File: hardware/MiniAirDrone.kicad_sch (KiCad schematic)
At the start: 29 parts, among them J1 USB_C_Receptacle_USB2.0, Q1 UMH3N, U1 CH340C, U2 ESP32-WROOM-32, U3 MPU-6050, U4 MS5611-01BA, U5 VL53L1CXV0FY1, U6 TS1117BCW33_RPG

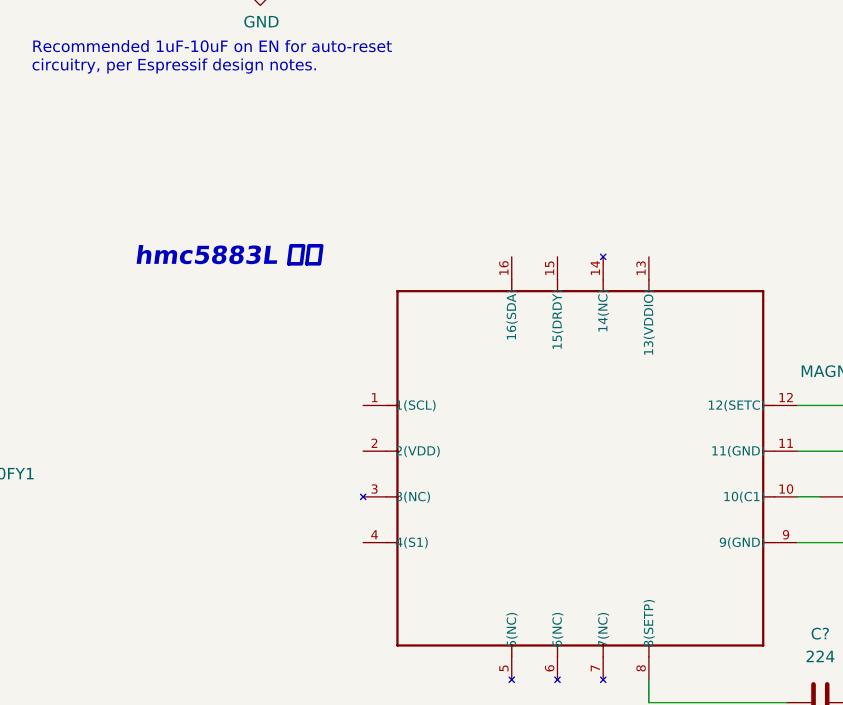
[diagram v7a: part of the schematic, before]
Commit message: Update MiniAirDrone.kicad_sch
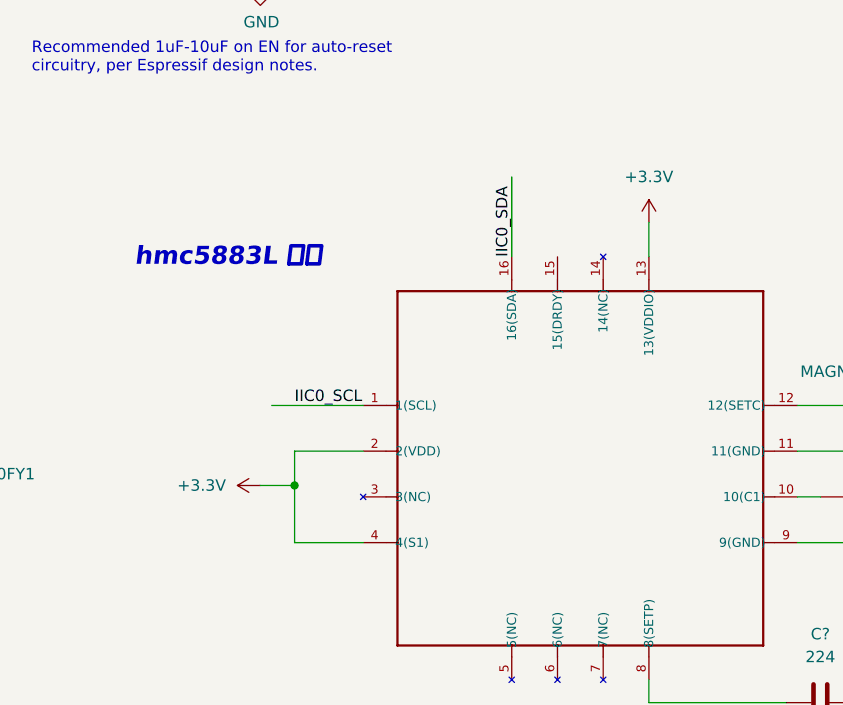
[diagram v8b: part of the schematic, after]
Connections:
- net +3.3V: now also U?.13 (13(VDDIO)), U?.2 (2(VDD)), U?.4 (4(S1))
- net IIC0_SCL: now also U?.1 (1(SCL))
- net IIC0_SDA: now also U?.16 (16(SDA))
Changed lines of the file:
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@@
   (junction (at 185.42 53.34) (diameter 0) (color 0 0 0 0)
+  )
+  (junction (at 241.3 109.22) (diameter 0) (color 0 0 0 0)
   )
   (junction (at 50.8 91.44) (diameter 0) (color 0 0 0 0)
@@
     (stroke (width 0) (type default) (color 0 0 0 0))
   )
+  (wire (pts (xy 241.3 115.57) (xy 241.3 109.22))
+    (stroke (width 0) (type default) (color 0 0 0 0))
+  )
+  (wire (pts (xy 238.76 100.33) (xy 248.92 100.33))
+    (stroke (width 0) (type default) (color 0 0 0 0))
+  )
   (wire (pts (xy 373.38 77.47) (xy 392.43 77.47))
     (stroke (width 0) (type default) (color 0 0 0 0))
@@
     (stroke (width 0) (type default) (color 0 0 0 0))
   )
+  (wire (pts (xy 265.43 74.93) (xy 265.43 83.82))
+    (stroke (width 0) (type default) (color 0 0 0 0))
+  )
   (wire (pts (xy 367.03 146.05) (xy 367.03 148.59))
     (stroke (width 0) (type default) (color 0 0 0 0))
@@
     (stroke (width 0) (type default) (color 0 0 0 0))
   )
+  (wire (pts (xy 280.67 80.01) (xy 280.67 83.82))
+    (stroke (width 0) (type default) (color 0 0 0 0))
+  )
   (wire (pts (xy 358.14 107.95) (xy 358.14 110.49))
     (stroke (width 0) (type default) (color 0 0 0 0))
@@
     (stroke (width 0) (type default) (color 0 0 0 0))
   )
+  (wire (pts (xy 248.92 115.57) (xy 241.3 115.57))
+    (stroke (width 0) (type default) (color 0 0 0 0))
+  )
   (wire (pts (xy 34.29 67.31) (xy 26.67 67.31))
     (stroke (width 0) (type default) (color 0 0 0 0))
@@
     (stroke (width 0) (type default) (color 0 0 0 0))
   )
+  (wire (pts (xy 241.3 105.41) (xy 248.92 105.41))
+    (stroke (width 0) (type default) (color 0 0 0 0))
+  )
   (wire (pts (xy 297.18 115.57) (xy 308.61 115.57))
     (stroke (width 0) (type default) (color 0 0 0 0))
@@
     (stroke (width 0) (type default) (color 0 0 0 0))
   )
+  (wire (pts (xy 241.3 109.22) (xy 241.3 105.41))
+    (stroke (width 0) (type default) (color 0 0 0 0))
+  )
   (wire (pts (xy 129.54 115.57) (xy 116.84 115.57))
     (stroke (width 0) (type default) (color 0 0 0 0))
@@
   )
   (wire (pts (xy 339.09 30.48) (xy 330.2 30.48))
+    (stroke (width 0) (type default) (color 0 0 0 0))
+  )
+  (wire (pts (xy 237.49 109.22) (xy 241.3 109.22))
     (stroke (width 0) (type default) (color 0 0 0 0))
   )
@@
     (effects (font (size 1.27 1.27)) (justify right bottom))
   )
+  (label "IIC0_SCL" (at 241.3 100.33 0)
+    (effects (font (size 1.27 1.27)) (justify left bottom))
+  )
   (label "IIC0_SDA" (at 96.52 101.6 0)
     (effects (font (size 1.27 1.27)) (justify left bottom))
@@
   )
   (label "IIC0_SDA" (at 168.91 106.68 0)
+    (effects (font (size 1.27 1.27)) (justify left bottom))
+  )
+  (label "IIC0_SDA" (at 265.43 83.82 90)
     (effects (font (size 1.27 1.27)) (justify left bottom))
   )
@@
     (pin "1")
     (pin "2")
+  )
+  (symbol (lib_id "power:+3.3V") (at 237.49 109.22 90) (unit 1)
+    (in_bom yes) (on_board yes) (fields_autoplaced)
+    (property "Reference" "#PWR?" (id 0) (at 241.3 109.22 0)
+      (effects (font (size 1.27 1.27)) hide)
+    )
+    (property "Value" "+3.3V" (id 1) (at 233.68 109.2199 90)
+      (effects (font (size 1.27 1.27)) (justify left))
+    )
+    (property "Footprint" "" (id 2) (at 237.49 109.22 0)
+      (effects (font (size 1.27 1.27)) hide)
+    )
+    (property "Datasheet" "" (id 3) (at 237.49 109.22 0)
+      (effects (font (size 1.27 1.27)) hide)
+    )
+    (pin "1")
+  )
+  (symbol (lib_id "power:+3.3V") (at 280.67 80.01 0) (unit 1)
+    (in_bom yes) (on_board yes) (fields_autoplaced)
+    (property "Reference" "#PWR?" (id 0) (at 280.67 83.82 0)
+      (effects (font (size 1.27 1.27)) hide)
+    )
+    (property "Value" "+3.3V" (id 1) (at 280.67 74.93 0))
+    (property "Footprint" "" (id 2) (at 280.67 80.01 0)
+      (effects (font (size 1.27 1.27)) hide)
+    )
+    (property "Datasheet" "" (id 3) (at 280.67 80.01 0)
+      (effects (font (size 1.27 1.27)) hide)
+    )
+    (pin "1")
   )
   (symbol (lib_id "power:GND") (at 325.12 33.02 0) (unit 1)
@@
       (reference "#PWR0104") (unit 1) (value "+3.3V") (footprint "")
     )
+    (path "/09fe4079-9258-4c47-a9ae-7c6f28880ea7"
+      (reference "#PWR?") (unit 1) (value "+3.3V") (footprint "")
+    )
+    (path "/12ef7f61-9f6f-48c6-88a3-b38c88233478"
+      (reference "#PWR?") (unit 1) (value "+3.3V") (footprint "")
+    )
     (path "/1cee6a59-d3a0-4f59-bd50-d39a8b45bae5"
